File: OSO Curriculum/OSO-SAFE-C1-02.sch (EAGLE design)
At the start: 17 parts, among them U1 LM1117T-3.3, U2 ATSAMD11D14A-SSNT

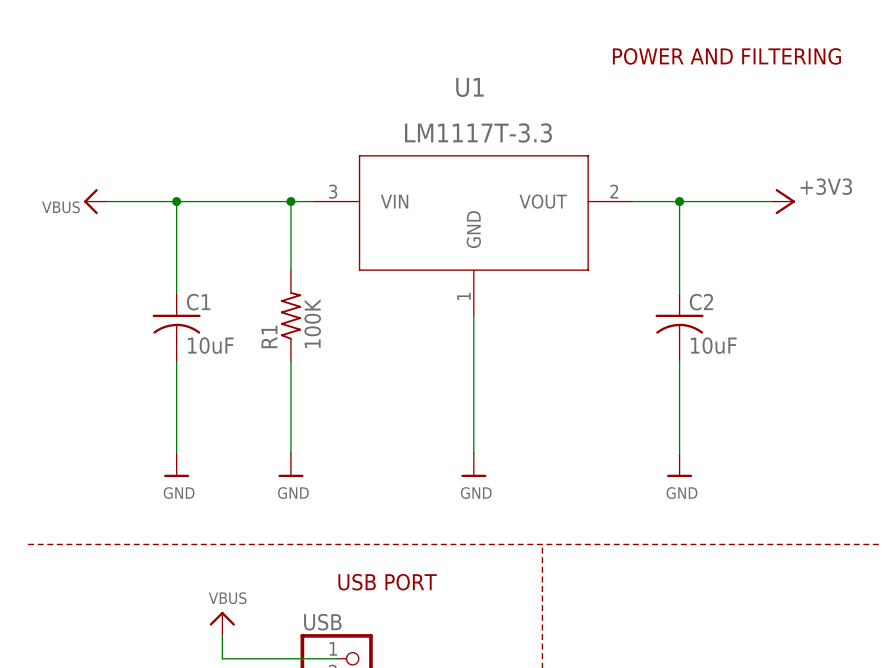
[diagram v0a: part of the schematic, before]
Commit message: update SAMD11 feathers
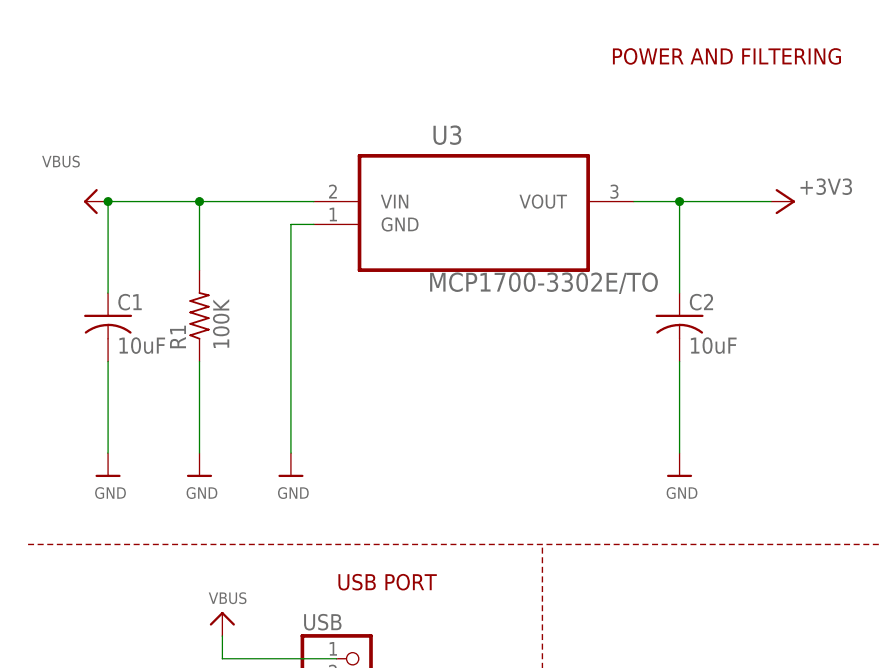
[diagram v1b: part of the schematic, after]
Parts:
- removed U1: LM1117T-3.3, My Stuff:LM1117T-3.3/NOPB
- added U3: MCP1700-3302E/TO, MCP1700-3302E_TO:MCP1700-3302E/TO
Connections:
- net +3V3: now also U3.VOUT; no longer U1.VOUT
- net GND: now also U3.GND; no longer U1.GND
- net VBUS: now also U3.VIN; no longer U1.VIN
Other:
- moved on the sheet: C1, R1
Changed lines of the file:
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@@
 <setting verticaltext="up"/>
 </settings>
-<grid distance="0.1" unitdist="inch" unit="inch" style="lines" multiple="1" display="no" altdistance="0.05" altunitdist="inch" altunit="inch"/>
+<grid distance="0.1" unitdist="inch" unit="inch" style="lines" multiple="1" display="no" altdistance="0.01" altunitdist="inch" altunit="inch"/>
 <layers>
 <layer number="1" name="Top" color="4" fill="1" visible="no" active="no"/>
@@
 <part name="+3V3" library="supply1" deviceset="+3V3" device=""/>
 <part name="U$3" library="microbuilder" deviceset="VBUS" device=""/>
-<part name="U1" library="My Stuff" deviceset="LM1117T-3.3/NOPB" device="" value="LM1117T-3.3"/>
 <part name="USB" library="pinhead" library_urn="urn:adsk.eagle:library:325" deviceset="PINHD-1X5" device="" package3d_urn="urn:adsk.eagle:package:22469/2"/>
 <part name="U$4" library="microbuilder" deviceset="GND" device=""/>
@@
 <part name="U$2" library="microbuilder" deviceset="GND" device=""/>
 <part name="U$10" library="microbuilder" deviceset="MOUNTINGHOLE" device="2.5"/>
+<part name="U3" library="MCP1700-3302E_TO" deviceset="MCP1700-3302E/TO" device=""/>
 </parts>
 <sheets>
@@
 <attribute name="SHEET" x="228.473" y="5.08" size="2.54" layer="94"/>
 </instance>
-<instance part="U$27" gate="G$1" x="20.32" y="124.46" smashed="yes">
-<attribute name="VALUE" x="18.796" y="121.92" size="1.27" layer="96"/>
+<instance part="U$27" gate="G$1" x="12.7" y="124.46" smashed="yes">
+<attribute name="VALUE" x="11.176" y="121.92" size="1.27" layer="96"/>
 </instance>
 <instance part="U$28" gate="G$1" x="200.66" y="124.46" smashed="yes">
@@
 <attribute name="VALUE" x="74.676" y="121.92" size="1.27" layer="96"/>
 </instance>
-<instance part="U$30" gate="G$1" x="53.34" y="124.46" smashed="yes">
-<attribute name="VALUE" x="51.816" y="121.92" size="1.27" layer="96"/>
+<instance part="U$30" gate="G$1" x="33.02" y="124.46" smashed="yes">
+<attribute name="VALUE" x="31.496" y="121.92" size="1.27" layer="96"/>
 </instance>
 <instance part="+3V4" gate="G$1" x="88.9" y="154.94" smashed="yes" rot="MR90">
 <attribute name="VALUE" x="89.408" y="157.48" size="1.778" layer="96" rot="MR180"/>
 </instance>
-<instance part="U$25" gate="G$1" x="33.02" y="124.46" smashed="yes">
-<attribute name="VALUE" x="31.496" y="121.92" size="1.27" layer="96"/>
+<instance part="U$25" gate="G$1" x="22.86" y="124.46" smashed="yes">
+<attribute name="VALUE" x="21.336" y="121.92" size="1.27" layer="96"/>
 </instance>
 <instance part="U$1" gate="G$1" x="25.4" y="109.22" smashed="yes">
@@
 </instance>
 <instance part="U$3" gate="G$1" x="10.16" y="154.94" smashed="yes" rot="R90">
-<attribute name="VALUE" x="9.652" y="154.94" size="1.27" layer="96" rot="R180"/>
-</instance>
-<instance part="U1" gate="A" x="53.34" y="154.94" smashed="yes">
-<attribute name="NAME" x="51.1556" y="166.5986" size="2.0828" layer="95" ratio="6" rot="SR0"/>
-<attribute name="VALUE" x="45.4406" y="161.5186" size="2.0828" layer="96" ratio="6" rot="SR0"/>
+<attribute name="VALUE" x="9.652" y="160.02" size="1.27" layer="96" rot="R180"/>
 </instance>
 <instance part="USB" gate="A" x="40.64" y="99.06" smashed="yes">
@@
 <attribute name="VALUE" x="77.216" y="138.049" size="1.778" layer="96"/>
 </instance>
-<instance part="C1" gate="G$1" x="20.32" y="142.24" smashed="yes">
-<attribute name="NAME" x="21.336" y="142.875" size="1.778" layer="95"/>
-<attribute name="VALUE" x="21.336" y="138.049" size="1.778" layer="96"/>
-</instance>
-<instance part="R1" gate="G$1" x="33.02" y="142.24" smashed="yes" rot="R90">
-<attribute name="NAME" x="31.5214" y="138.43" size="1.778" layer="95" rot="R90"/>
-<attribute name="VALUE" x="36.322" y="138.43" size="1.778" layer="96" rot="R90"/>
+<instance part="C1" gate="G$1" x="12.7" y="142.24" smashed="yes">
+<attribute name="NAME" x="13.716" y="142.875" size="1.778" layer="95"/>
+<attribute name="VALUE" x="13.716" y="138.049" size="1.778" layer="96"/>
+</instance>
+<instance part="R1" gate="G$1" x="22.86" y="142.24" smashed="yes" rot="R90">
+<attribute name="NAME" x="21.3614" y="138.43" size="1.778" layer="95" rot="R90"/>
+<attribute name="VALUE" x="26.162" y="138.43" size="1.778" layer="96" rot="R90"/>
 </instance>
 <instance part="RESET" gate="G$1" x="38.1" y="15.24" smashed="yes">
@@
 </instance>
 <instance part="U$10" gate="G$1" x="243.84" y="27.94" smashed="yes"/>
+<instance part="U3" gate="A" x="53.34" y="157.48" smashed="yes">
+<attribute name="NAME" x="48.62831875" y="161.274809375" size="2.088409375" layer="95" ratio="10" rot="SR0"/>
+<attribute name="VALUE" x="48.22593125" y="144.9366" size="2.086340625" layer="96" ratio="10" rot="SR0"/>
+</instance>
 </instances>
 <busses>
@@
 <segment>
 <pinref part="U$27" gate="G$1" pin="GND"/>
-<wire x1="20.32" y1="137.16" x2="20.32" y2="127" width="0.1524" layer="91"/>
+<wire x1="12.7" y1="137.16" x2="12.7" y2="127" width="0.1524" layer="91"/>
 <pinref part="C1" gate="G$1" pin="2"/>
 </segment>
@@
 </segment>
 <segment>
-<wire x1="53.34" y1="142.24" x2="53.34" y2="127" width="0.1524" layer="91"/>
+<wire x1="33.02" y1="152.4" x2="33.02" y2="127" width="0.1524" layer="91"/>
 <pinref part="U$30" gate="G$1" pin="GND"/>
-<pinref part="U1" gate="A" pin="GND"/>
+<pinref part="U3" gate="A" pin="GND"/>
+<wire x1="35.56" y1="152.4" x2="33.02" y2="152.4" width="0.1524" layer="91"/>
 </segment>
 <segment>
 <pinref part="U$25" gate="G$1" pin="GND"/>
-<wire x1="33.02" y1="127" x2="33.02" y2="137.16" width="0.1524" layer="91"/>
+<wire x1="22.86" y1="127" x2="22.86" y2="137.16" width="0.1524" layer="91"/>
 <pinref part="R1" gate="G$1" pin="1"/>
 </segment>
@@
 <pinref part="R1" gate="G$1" pin="2"/>
 <pinref part="U$3" gate="G$1" pin="VBUS"/>
-<wire x1="12.7" y1="154.94" x2="20.32" y2="154.94" width="0.1524" layer="91"/>
-<wire x1="20.32" y1="154.94" x2="20.32" y2="144.78" width="0.1524" layer="91"/>
-<pinref part="U1" gate="A" pin="VIN"/>
+<wire x1="12.7" y1="154.94" x2="12.7" y2="144.78" width="0.1524" layer="91"/>
 <pinref part="C1" gate="G$1" pin="1"/>
-<junction x="20.32" y="154.94"/>
-<wire x1="20.32" y1="154.94" x2="33.02" y2="154.94" width="0.1524" layer="91"/>
-<wire x1="33.02" y1="154.94" x2="35.56" y2="154.94" width="0.1524" layer="91"/>
-<wire x1="33.02" y1="147.32" x2="33.02" y2="154.94" width="0.1524" layer="91"/>
-<junction x="33.02" y="154.94"/>
+<junction x="12.7" y="154.94"/>
+<wire x1="12.7" y1="154.94" x2="22.86" y2="154.94" width="0.1524" layer="91"/>
+<wire x1="22.86" y1="154.94" x2="35.56" y2="154.94" width="0.1524" layer="91"/>
+<wire x1="22.86" y1="147.32" x2="22.86" y2="154.94" width="0.1524" layer="91"/>
+<junction x="22.86" y="154.94"/>
+<pinref part="U3" gate="A" pin="VIN"/>
 </segment>
 <segment>
@@
 <segment>
 <pinref part="+3V4" gate="G$1" pin="+3V3"/>
-<pinref part="U1" gate="A" pin="VOUT"/>
 <wire x1="71.12" y1="154.94" x2="76.2" y2="154.94" width="0.1524" layer="91"/>
 <wire x1="76.2" y1="154.94" x2="86.36" y2="154.94" width="0.1524" layer="91"/>
@@
 <wire x1="76.2" y1="144.78" x2="76.2" y2="154.94" width="0.1524" layer="91"/>
 <pinref part="C2" gate="G$1" pin="1"/>
-</segment>
-<segment>
+<pinref part="U3" gate="A" pin="VOUT"/>
+</segment>
+<segment>
